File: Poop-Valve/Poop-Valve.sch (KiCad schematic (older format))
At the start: 30 parts

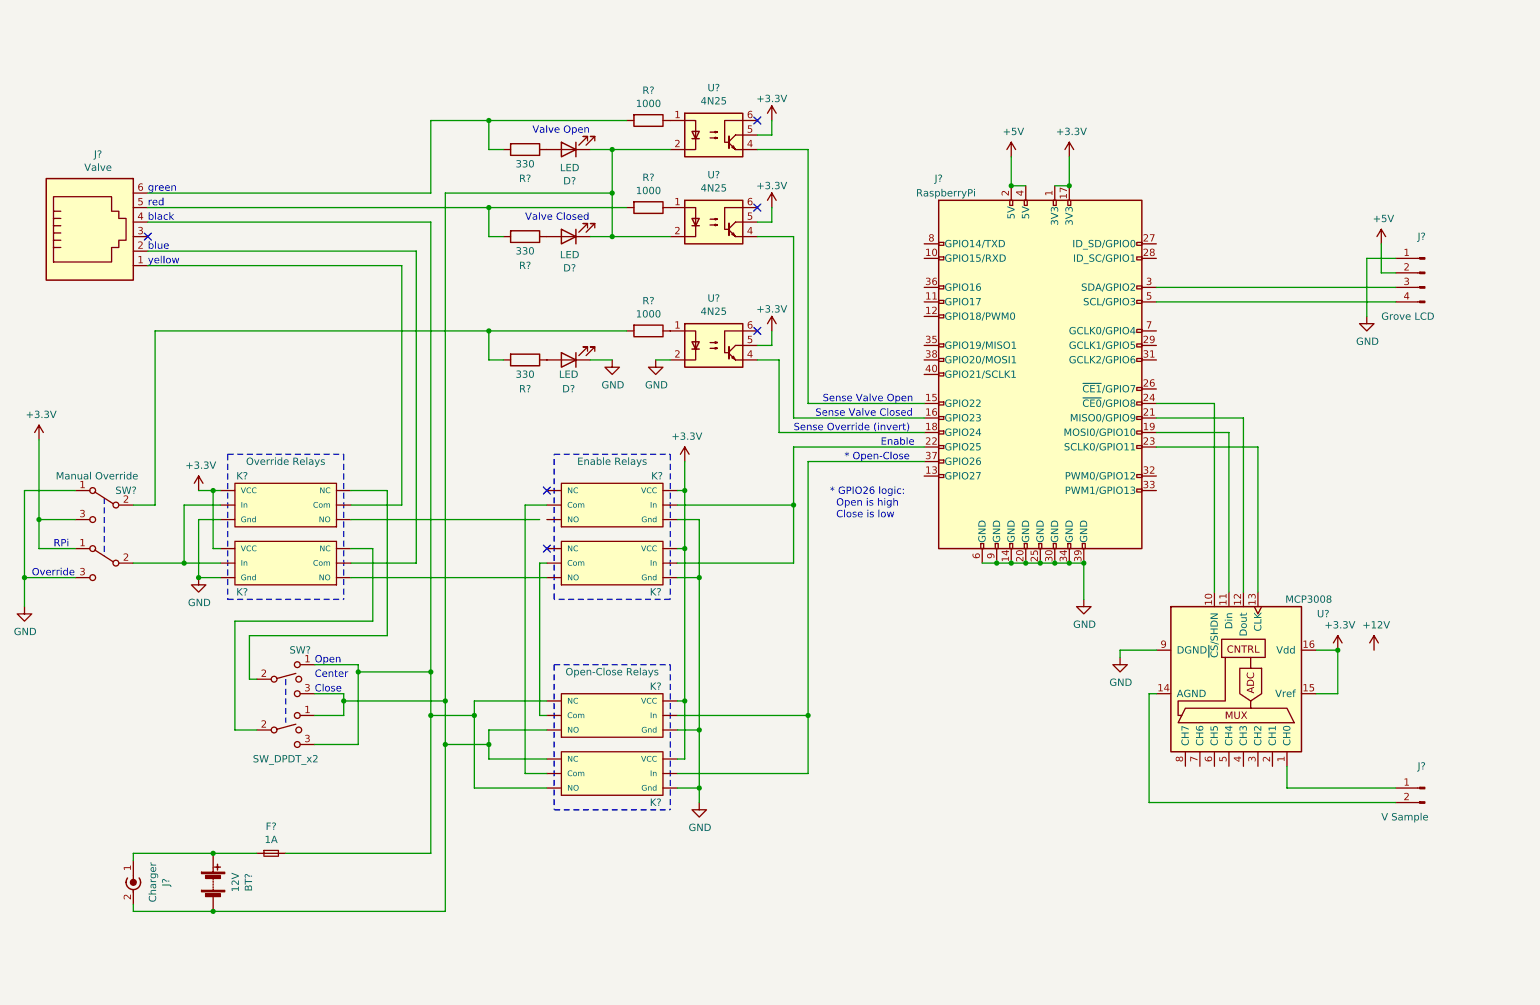
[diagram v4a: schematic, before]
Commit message: v0.5 add connectors
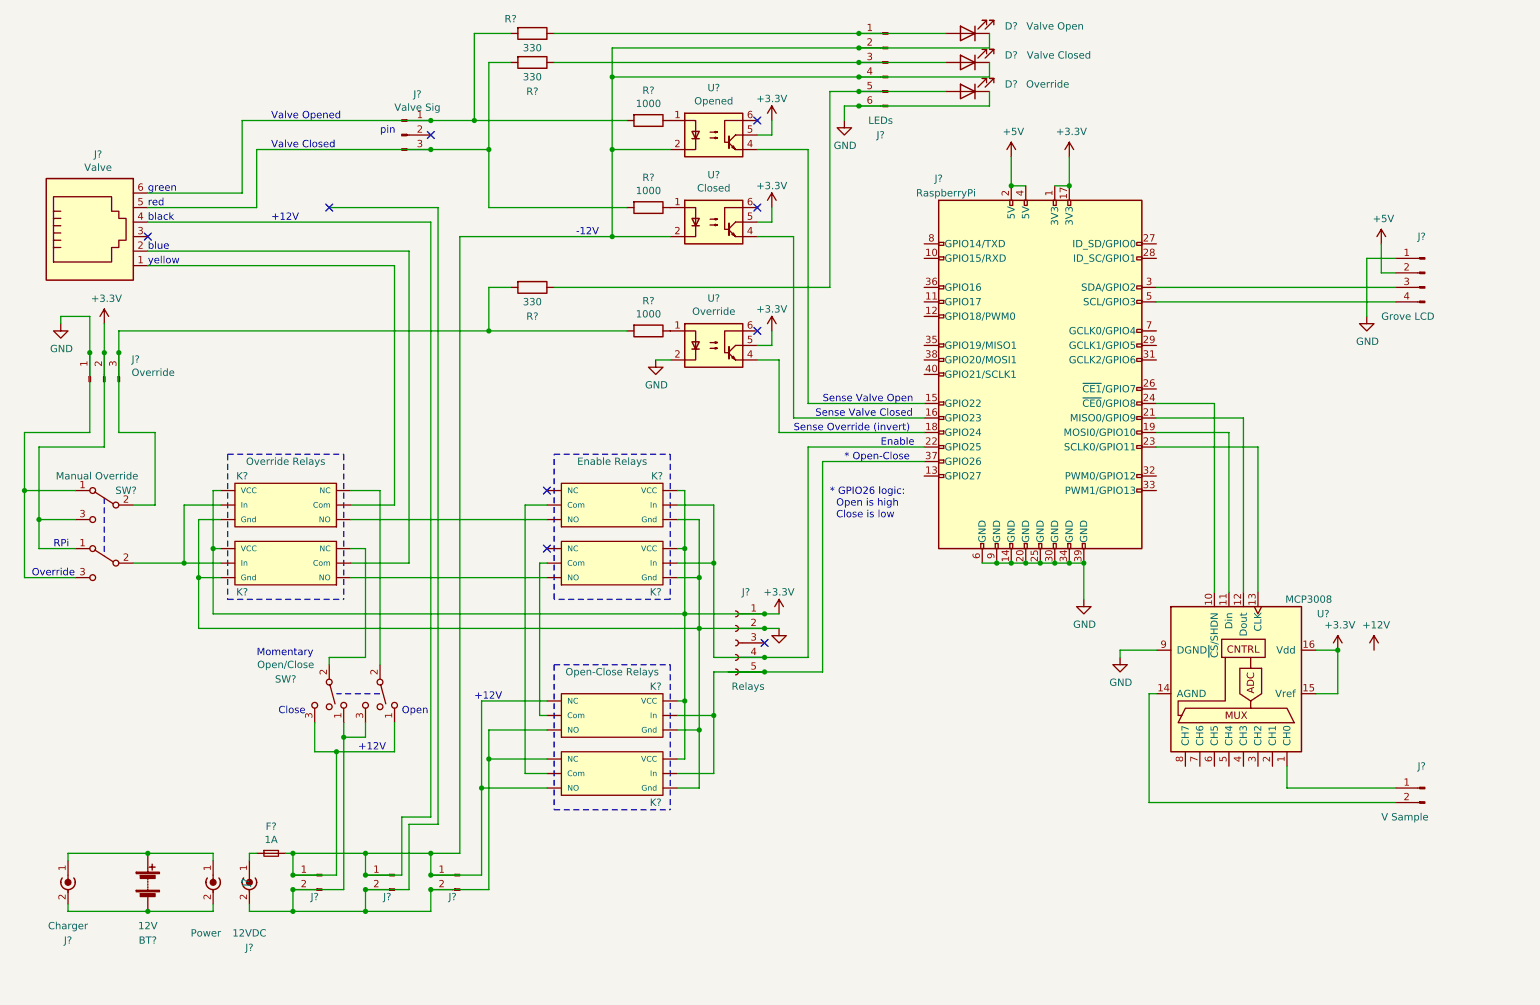
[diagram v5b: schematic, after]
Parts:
- removed SW? (x2): SW_DPDT_x2, symbol Switch:SW_SPDT_MSM
- added J?: Relays, symbol Connector:Conn_01x05_Female
- added J?: 12VDC, symbol Connector:Conn_Coaxial_Power
- added J?: Power, symbol Connector:Conn_Coaxial_Power
- added J? (x3): Conn_01x02_Male, symbol Connector:Conn_01x02_Male
- added J?: Override, symbol Connector:Conn_01x03_Male
- added J?: Valve Sig, symbol Connector:Conn_01x03_Male
- added J?: LEDs, symbol Connector:Conn_01x06_Male
- added SW?: Open/Close, symbol Switch:SW_SPDT_MSM
- added SW?: SW_DPDT_x2, symbol Switch:SW_SPDT_MSM
- D?: value LED -> Valve Closed
- D?: value LED -> Valve Open
- D?: value LED -> Override
- U?: value 4N25 -> Opened
- U?: value 4N25 -> Closed
- U?: value 4N25 -> Override
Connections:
- net +3V3: now also J?.1 (Pin_1), J?.2 (Pin_2)
- net GND: now also J?.1 (Pin_1), J?.2 (Pin_2), J?.6 (Pin_6)
- net at D?.1 (K), D?.1 (K), K?.~ (VCC)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: now also F?.2, J?.4, J?.1 (Pin_1), J?.1 (Pin_1), J?.1 (Pin_1), J?.2 (Pin_2), J?.4 (Pin_4), SW?.1, SW?.3; no longer BT?.2 (-), J?.2 (Ext)
- net at BT?.1 (+), J?.1 (In): now also J?.1 (In); no longer F?.1
- net at D?.2 (A), R?.1: now also J?.3 (Pin_3)
- net at D?.2 (A), R?.1: now also J?.1 (Pin_1)
- net at J?.5, R?.2, R?.2: now also J?.3 (Pin_3)
- net at J?.6, R?.2, R?.2: now also J?.1 (Pin_1)
- net at R?.2, R?.2, SW?.2 (B): now also J?.3 (Pin_3)
- net at D?.2 (A), R?.1: now also J?.5 (Pin_5)
- new net: J?.22 (GPIO25), J?.4 (Pin_4), K?.~ (VCC), K?.~ (VCC)
- new net: J?.37 (GPIO26), J?.5 (Pin_5), K?.~ (VCC), K?.~ (VCC)
- new net: K?.~ (VCC), K?.~ (VCC) (x4)
- new net: BT?.2 (-), J?.2 (Ext), J?.2 (Ext)
- new net: F?.1, J?.1 (In)
- new net: K?.~ (VCC), K?.~ (VCC), SW?.2 (B)
- new net: K?.~ (VCC), SW?.2 (x2)
- new net: J?.2 (Ext), J?.2 (Pin_2), J?.2 (Pin_2), J?.2 (Pin_2), K?.~ (VCC), K?.~ (VCC), SW?.1, SW?.3
- no-connect marks 6 -> 9
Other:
- note added: "+12V"
- note added: "-12V"
- note added: "Momentary"
- note added: "Valve Opened"
- note added: "pin"
- note removed: "Center"
- note removed: "Valve Open"
- moved on the sheet: BT?, D?, J?, R?
